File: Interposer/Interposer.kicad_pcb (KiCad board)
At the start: 2 copper layers, 55 x 52 mm, 5 parts

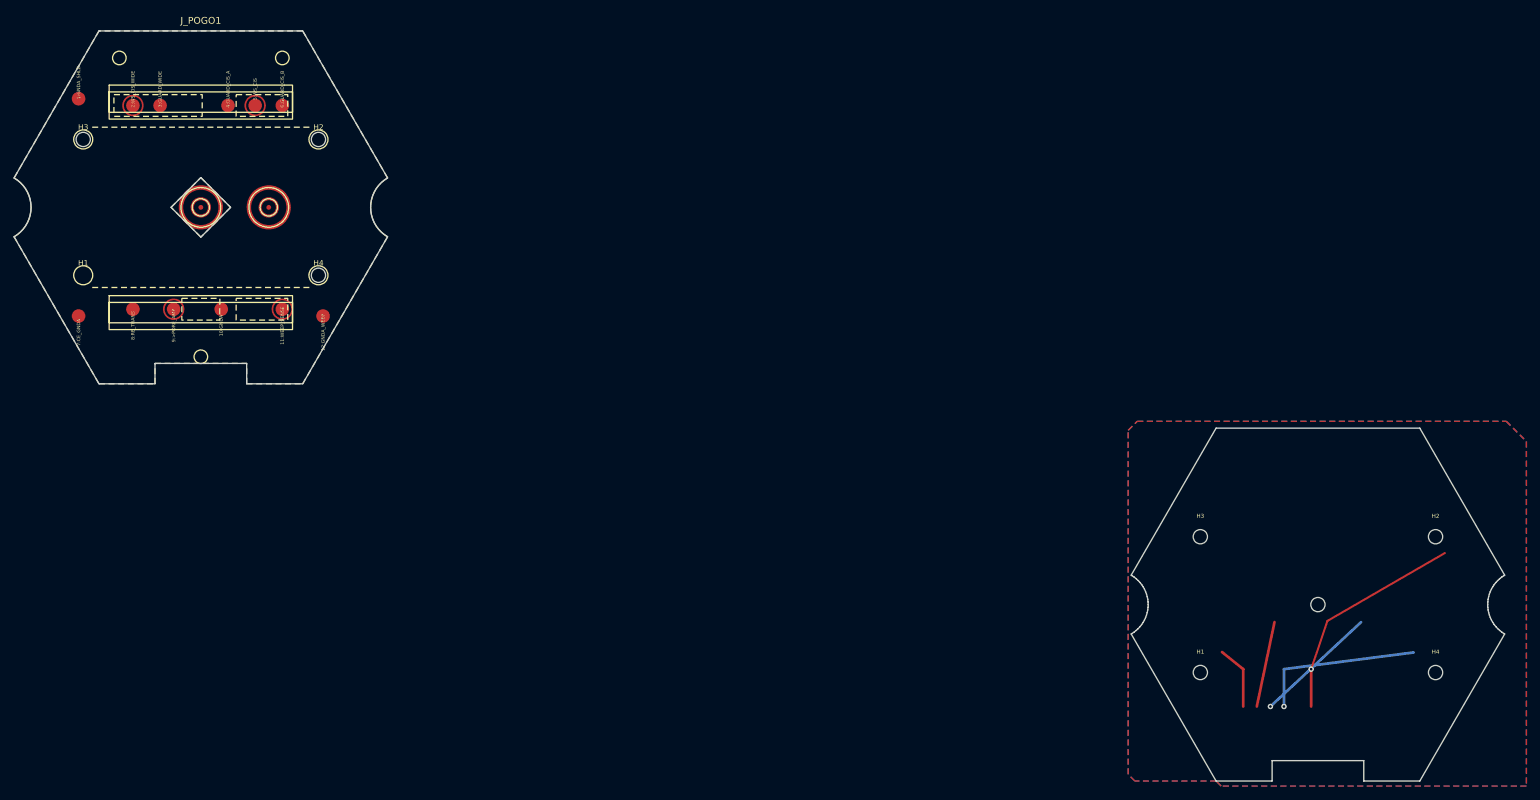
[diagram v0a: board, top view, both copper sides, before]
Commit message: Fix interposer fluid channel routing and update default footprints
Co-authored-by: google-labs-jules[bot] <161369871+google-labs-jules[bot]@users.noreply.github.com>
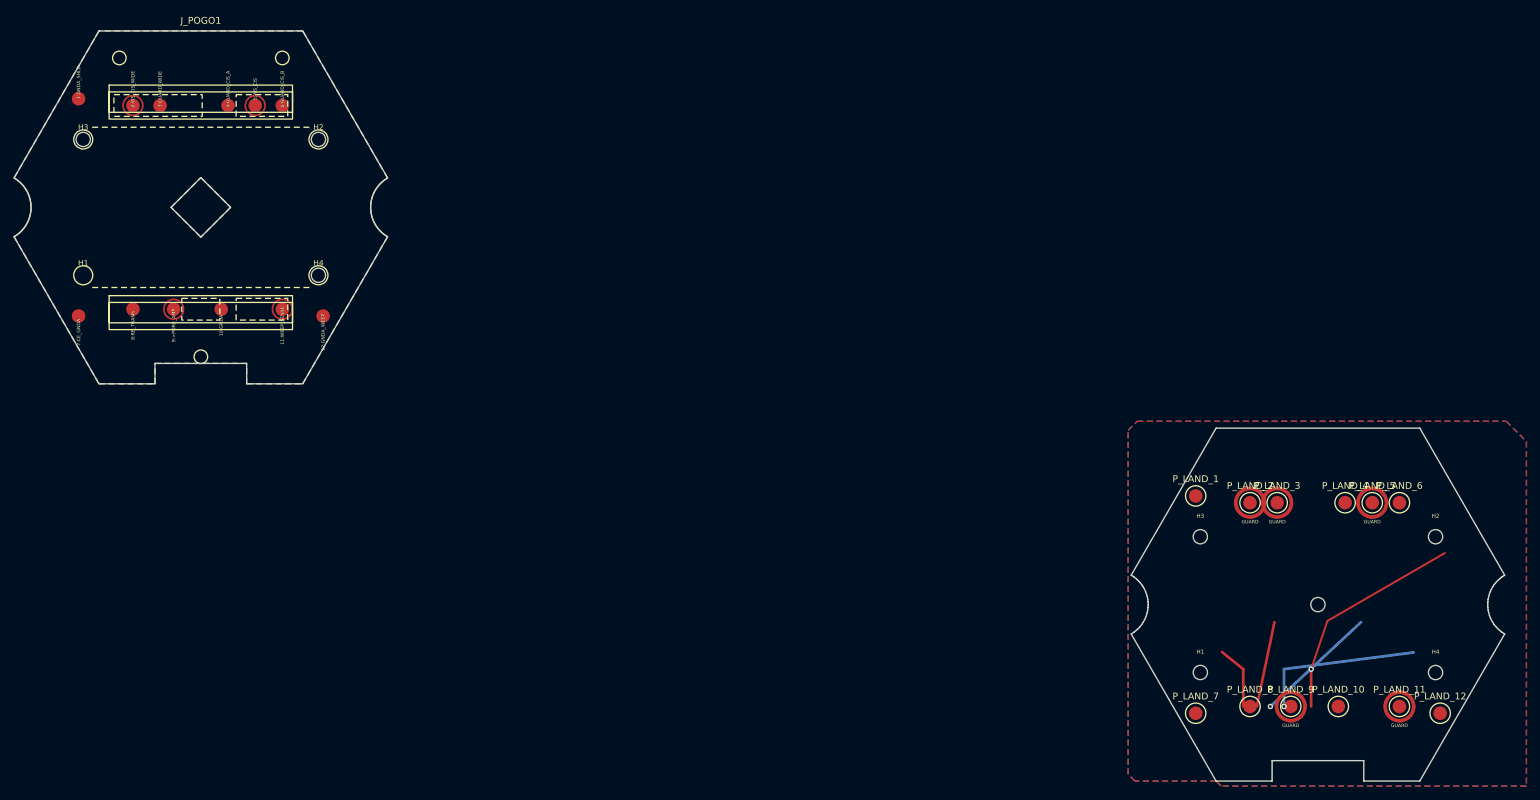
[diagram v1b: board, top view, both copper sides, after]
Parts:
- added P_LAND_1: GNDA_SHLD, PogoPin_Target_Landing_1Pin, F.Cu at (146.5, 42.5)
- added P_LAND_10: GNDA, PogoPin_Target_Landing_1Pin, F.Cu at (167.5, 73.5)
- added P_LAND_11: WEEP_SENSE, PogoPin_Target_Landing_1Pin_Guarded, F.Cu at (176.5, 73.5)
- added P_LAND_12: GNDA_WEEP, PogoPin_Target_Landing_1Pin, F.Cu at (182.5, 74.5)
- added P_LAND_2: WS_CIS_WIDE, PogoPin_Target_Landing_1Pin_Guarded, F.Cu at (154.5, 43.5)
- added P_LAND_3: GUARD_WIDE, PogoPin_Target_Landing_1Pin_Guarded, F.Cu at (158.5, 43.5)
- added P_LAND_4: GUARD_CIS_A, PogoPin_Target_Landing_1Pin, F.Cu at (168.5, 43.5)
- added P_LAND_5: WS_CIS, PogoPin_Target_Landing_1Pin_Guarded, F.Cu at (172.5, 43.5)
- added P_LAND_6: GUARD_CIS_B, PogoPin_Target_Landing_1Pin, F.Cu at (176.5, 43.5)
- added P_LAND_7: CE_GNDA, PogoPin_Target_Landing_1Pin, F.Cu at (146.5, 74.5)
- added P_LAND_8: RE_TRANS, PogoPin_Target_Landing_1Pin, F.Cu at (154.5, 73.5)
- added P_LAND_9: >PORE_AMP, PogoPin_Target_Landing_1Pin_Guarded, F.Cu at (160.5, 73.5)
